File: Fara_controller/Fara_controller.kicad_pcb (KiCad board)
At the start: 2 copper layers, 68.5 x 45.8 mm, 29 parts, among them U1 XL1509-12, U2 LDD-700L, U3 LDD-700L, U4 LDD-700L, U5 LDD-700L, X1 Conn_01x02, X10 Conn_01x02, X11 Conn_01x02, X2 Conn_01x02, X3 Fan_3pin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

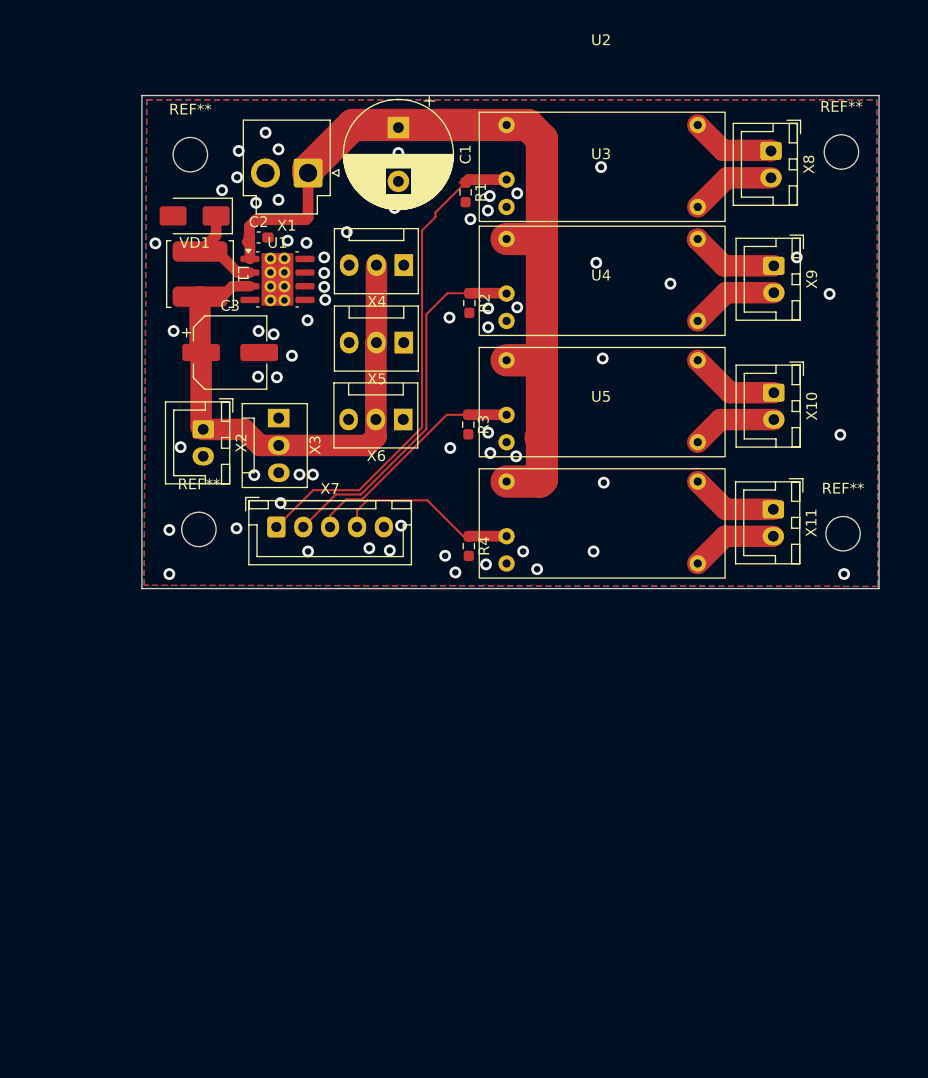
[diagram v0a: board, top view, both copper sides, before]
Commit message: v0.2 draft routing of the 24V edition
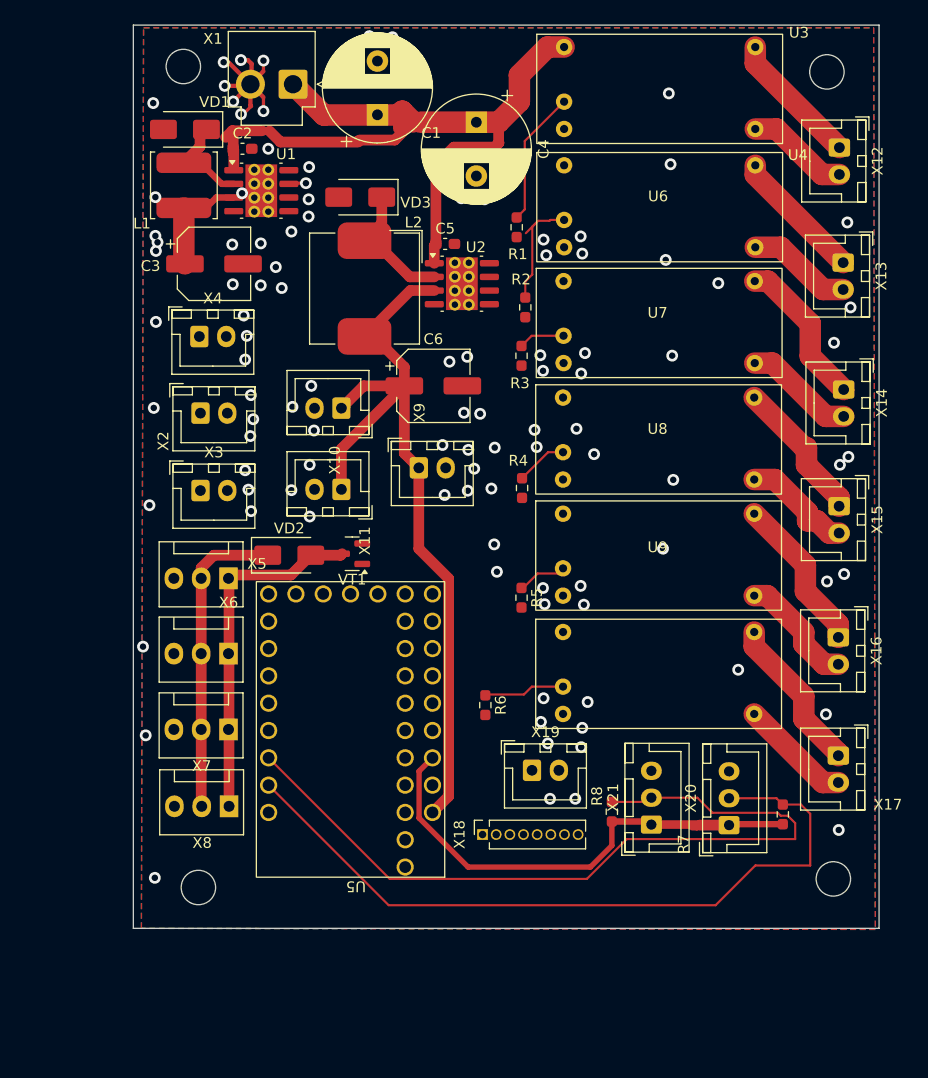
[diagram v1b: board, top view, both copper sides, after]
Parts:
- added C4: 470uF, Capacitor_THT:CP_Radial_D10.0mm_P5.00mm, F.Cu at (70.3, 18.3)
- added C5: 1u, Capacitor_SMD:C_0603_1608Metric_Pad1.08x0.95mm_HandSolder, F.Cu at (67.4, 29.6)
- added C6: 180uF, Capacitor_SMD:CP_Elec_6.3x7.7, F.Cu at (66.3, 42.8)
- added L2: 68uH, Inductor_SMD:L_Bourns_SRP1050WA, F.Cu at (59.9, 33.8)
- added R5: 10k, Resistor_SMD:R_0603_1608Metric_Pad0.98x0.95mm_HandSolder, F.Cu at (74.5, 62.5)
- added R6: 10k, Resistor_SMD:R_0603_1608Metric_Pad0.98x0.95mm_HandSolder, F.Cu at (71.1, 72.5)
- added R7: 4k7, Resistor_SMD:R_0603_1608Metric_Pad0.98x0.95mm_HandSolder, F.Cu at (98.8, 82.7)
- added R8: 4k7, Resistor_SMD:R_0603_1608Metric_Pad0.98x0.95mm_HandSolder, F.Cu at (82.9, 82.4)
- added U6: LDD-700L, my8lib:LDD-700L, F.Cu at (87.3, 36.9)
- added U7: LDD-700L, my8lib:LDD-700L, F.Cu at (87.2, 47.7)
- added U8: LDD-700L, my8lib:LDD-700L, F.Cu at (87.2, 58.5)
- added U9: LDD-700L, my8lib:LDD-700L, F.Cu at (87.2, 69.5)
- added VD2: CDBA3100-HF, Diode_SMD:D_SMA, F.Cu at (52.9, 58.5)
- added VD3: CDBA3100-HF, Diode_SMD:D_SMA, F.Cu at (59.5, 25.2)
- added VT1: AO3400A, Package_TO_SOT_SMD:SOT-23, F.Cu at (58.8, 58.4)
- added X12: Conn_01x02, Connector_JST:JST_XH_B2B-XH-A_1x02_P2.50mm_Vertical, F.Cu at (104.1, 20.6)
- added X13: Conn_01x02, Connector_JST:JST_XH_B2B-XH-A_1x02_P2.50mm_Vertical, F.Cu at (104.4, 31.3)
- added X14: Conn_01x02, Connector_JST:JST_XH_B2B-XH-A_1x02_P2.50mm_Vertical, F.Cu at (104.5, 43.1)
- added X15: Conn_01x02, Connector_JST:JST_XH_B2B-XH-A_1x02_P2.50mm_Vertical, F.Cu at (104.0, 54.0)
- added X16: Conn_01x02, Connector_JST:JST_XH_B2B-XH-A_1x02_P2.50mm_Vertical, F.Cu at (104.0, 66.2)
- added X17: Conn_01x02, Connector_JST:JST_XH_B2B-XH-A_1x02_P2.50mm_Vertical, F.Cu at (104.0, 77.2)
- added X18: Objective, Connector_PinSocket_1.27mm:PinSocket_1x08_P1.27mm_Vertical, F.Cu at (70.9, 84.5)
- added X19: Conn_01x02, Connector_JST:JST_XH_B2B-XH-A_1x02_P2.50mm_Vertical, F.Cu at (75.5, 78.5)
- added X20: Conn_01x03, Connector_JST:JST_XH_B3B-XH-A_1x03_P2.50mm_Vertical, F.Cu at (93.8, 83.7)
- added X21: Conn_01x03, Connector_JST:JST_XH_B3B-XH-A_1x03_P2.50mm_Vertical, F.Cu at (86.6, 83.6)
- U2: value LDD-700L -> XL1509-05; footprint my8lib:LDD-700L -> Package_SO:SOIC-8-1EP_3.9x4.9mm_P1.27mm_EP2.95x4.9mm_Mask2.71x3.4mm_ThermalVias
- U5: value LDD-700L -> ~; footprint my8lib:LDD-700L -> my8lib:RP2040Zero
- X3, X4: value Fan_3pin -> Conn_01x02; footprint Connector:FanPinHeader_1x03_P2.54mm_Vertical -> Connector_JST:JST_XH_B2B-XH-A_1x02_P2.50mm_Vertical
- X7: value Joystick -> Fan_3pin; footprint Connector_JST:JST_XH_B5B-XH-A_1x05_P2.50mm_Vertical -> Connector:FanPinHeader_1x03_P2.54mm_Vertical
- X8: value Conn_01x02 -> Fan_3pin; footprint Connector_JST:JST_XH_B2B-XH-A_1x02_P2.50mm_Vertical -> Connector:FanPinHeader_1x03_P2.54mm_Vertical
- moved X8 79.1 mm to (47.3, 81.9), turned to 180 degrees
- moved X10 40.2 mm to (57.8, 44.9), turned to 180 degrees
- moved X11 40.2 mm to (57.8, 52.4), turned to 180 degrees
- moved X9 38.0 mm to (65.0, 50.4), turned to 0 degrees
- moved REF** 33.3 mm to (44.5, 89.5)
- moved REF** 32.1 mm to (103.5, 88.7)
- moved U5 30.4 mm to (58.6, 74.8), turned to 180 degrees
- moved X5 27.3 mm to (47.2, 60.7)
- moved X6 27.2 mm to (47.2, 67.7)
- moved X4 20.1 mm to (44.5, 38.2), turned to 0 degrees
- moved X7 19.3 mm to (47.2, 74.8), turned to 180 degrees
- moved U4 18.9 mm to (87.3, 26.1)
- moved U3 18.6 mm to (87.3, 15.1)
- moved U2 17.0 mm to (69.0, 33.3)
- moved X3 9.92 mm to (44.6, 52.5), turned to 0 degrees
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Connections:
- R1 pad 1: Net-(U2-PWM) -> LEDS1
- R2 pad 1: Net-(U3-PWM) -> LEDS2
- R3 pad 1: Net-(U4-PWM) -> LEDS3
- R4 pad 1: Net-(U5-PWM) -> LEDS4
- U2 pad 2: Net-(U2-PWM) -> Net-(U2-OUT)
- U2 pad 3: GND -> +5V
- U2 pad 4: Net-(U2-Vout-) -> GND
- U2 pad 5: Net-(U2-Vout+) -> GND
- U3 pad 2: Net-(U3-PWM) -> LEDS1
- U4 pad 2: Net-(U4-PWM) -> LEDS2
- U5 pad 1: VPP -> therm1
- U5 pad 2: Net-(U5-PWM) -> therm2
- U5 pad 3: GND -> LEDS1
- U5 pad 4: Net-(U5-Vout-) -> LEDS2
- U5 pad 5: Net-(U5-Vout+) -> LEDS3
- X10 pad 1: Net-(U4-Vout+) -> +5V
- X10 pad 2: Net-(U4-Vout-) -> GND
- X11 pad 1: Net-(U5-Vout+) -> +5V
- X11 pad 2: Net-(U5-Vout-) -> GND
- X3 pad 1: unconnected-(X3-Tacho-Pad1) -> +12V
- X3 pad 2: +12V -> GND
- X4 pad 1: unconnected-(X4-Tacho-Pad1) -> +12V
- X4 pad 2: +12V -> GND
- X5 pad 1: unconnected-(X5-Tacho-Pad1) -> Net-(VD2-A)
- X5 pad 3: GND -> unconnected-(X5---Pad3)
- X6 pad 1: unconnected-(X6-Tacho-Pad1) -> Net-(VD2-A)
- X6 pad 3: GND -> unconnected-(X6---Pad3)
- X7 pad 1: Net-(U2-PWM) -> Net-(VD2-A)
- X7 pad 2: Net-(U3-PWM) -> +12V
- X7 pad 3: Net-(U4-PWM) -> unconnected-(X7---Pad3)
- X8 pad 1: Net-(U2-Vout+) -> Net-(VD2-A)
- X8 pad 2: Net-(U2-Vout-) -> +12V
- X9 pad 1: Net-(U3-Vout+) -> +5V
- X9 pad 2: Net-(U3-Vout-) -> GND
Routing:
- net +5V: track 0.00 -> 76.5 mm
- net therm2: track 0.00 -> 74.8 mm
- net therm1: track 0.00 -> 69.5 mm
- net Net-(U2-PWM): track 46.3 -> 0.00 mm
- net +3.3V: track 0.00 -> 45.9 mm
- net Net-(U3-PWM): track 34.2 -> 0.00 mm
- net Net-(VD2-A): track 0.00 -> 32.7 mm
- net Net-(U4-PWM): track 21.4 -> 0.00 mm
- net GND: track 0.00 -> 21.1 mm, vias 67 -> 112
- net Net-(U5-PWM): track 17.3 -> 0.00 mm
- net Net-(U9-Vout+): track 0.00 -> 14.7 mm
- net Net-(U8-Vout+): track 0.00 -> 14.7 mm
- net Net-(U6-Vout+): track 0.00 -> 14.2 mm
- net Net-(U7-Vout+): track 0.00 -> 13.5 mm
- net LEDS1: track 0.00 -> 12.6 mm
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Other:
- board size 68.5 x 45.8 mm -> 69.3 x 84 mm
- board text added: "Платка Рахилы 70 х 110 мм"

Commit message: v0.3 Seems 2B ready
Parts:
- moved X19 21.8 mm to (63.7, 96.9)
- moved REF** 17.0 mm to (32.0, 101.0)
- moved REF** 16.2 mm to (32.0, 25.0)
- moved R8 15.8 mm to (72.5, 94.3)
- moved REF** 15.6 mm to (94.0, 101.0)
- moved U2 15.6 mm to (58.9, 45.2)
- moved U5 15.6 mm to (48.5, 86.8)
- moved X9 15.6 mm to (54.9, 62.3)
- moved C1 15.6 mm to (51.0, 29.5)
- moved C6 15.6 mm to (56.2, 54.7)
- moved U6 15.6 mm to (77.2, 48.8)
- moved U8 15.6 mm to (77.2, 70.4)
- moved U9 15.6 mm to (77.2, 81.4)
- moved VD1 15.6 mm to (33.1, 30.9)
- moved VD2 15.6 mm to (42.9, 70.5)
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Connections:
- U5 pad 0: FAN -> unconnected-(U5-GP0/TX0/SDA0/MISO0-Pad0)
- U5 pad 12: unconnected-(U5-GP12/TX0/SDA0/MISO1-Pad12) -> FAN
- U5 pad 13: unconnected-(U5-GP13/RX0/SCL0/CS1-Pad13) -> STROBE_INPUT
- U5 pad 14: unconnected-(U5-GP14/SDA1/SCK1-Pad14) -> LEDS6
- U5 pad 15: unconnected-(U5-GP15/SCL1/MOSI1-Pad15) -> LEDS5
- U5 pad 26: unconnected-(U5-GP26/ADC0/SDA1-Pad26) -> LEDS4
- U5 pad 27: unconnected-(U5-GP27/ADC1/SCL1-Pad27) -> LEDS3
- U5 pad 28: unconnected-(U5-GP28/ADC2-Pad28) -> LEDS2
- U5 pad 29: unconnected-(U5-GP29/ADC3-Pad29) -> LEDS1
- U5 pad 3: LEDS1 -> unconnected-(U5-GP3/SCL1/MOSI0-Pad3)
- U5 pad 4: LEDS2 -> unconnected-(U5-GP4/TX1/SDA0/MIOS0-Pad4)
- U5 pad 5: LEDS3 -> unconnected-(U5-GP5/RX1/SCL0/CS0-Pad5)
- U5 pad 6: LEDS4 -> unconnected-(U5-GP6/SDA1/SCK1-Pad6)
- U5 pad 7: LEDS5 -> unconnected-(U5-GP7/SCL1/MOSI0-Pad7)
- U5 pad 8: LEDS6 -> unconnected-(U5-GP8/TX1/SDA0/MISO1-Pad8)
- U5 pad 9: STROBE_INPUT -> unconnected-(U5-GP9/RX1/CS1-Pad9)
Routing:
- net VPP: track 72.0 -> 148.5 mm
- net LEDS1: track 12.6 -> 73.2 mm
- net LEDS2: track 11.5 -> 65.6 mm
- net LEDS3: track 4.30 -> 58.3 mm
- net LEDS4: track 4.81 -> 52.3 mm
- net LEDS5: track 4.61 -> 45.2 mm
- net STROBE_INPUT: track 0.00 -> 36.9 mm
- net LEDS6: track 7.75 -> 40.1 mm
- net +12V: track 39.2 -> 70.2 mm
- net therm1: track 69.5 -> 64.3 mm
- net FAN: track 0.00 -> 3.99 mm
- net GND: vias 112 -> 142
